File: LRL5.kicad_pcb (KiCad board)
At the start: 2 copper layers, 140 x 50 mm, 33 parts, among them J1 POWER, J2 On/Off, J5 OUT, J6 MODE, J7 ADJUST, Q1 BC549, U1 BA033CC0T, U2 NHD-C0220BIZ

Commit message: Change some pins so thay don't interact with JTAG
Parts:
- moved R8 2.00 mm to (176.2, 56.2), turned to 180 degrees
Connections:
- J3 pad 10: ADJUST_B -> unconnected-(J3-Pin_10-Pad10)
- J3 pad 11: FOUT -> unconnected-(J3-Pin_11-Pad11)
- J3 pad 12: unconnected-(J3-Pin_12-Pad12) -> MODE_B
- J3 pad 13: unconnected-(J3-Pin_13-Pad13) -> ADJUST_B
- J3 pad 9: MODE_B -> unconnected-(J3-Pin_9-Pad9)
- J4 pad 16: unconnected-(J4-Pin_16-Pad16) -> FOUT
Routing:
- net FOUT: track 26.6 -> 56.2 mm, vias 1 -> 2
- net MODE_B: track 110.9 -> 103.3 mm
- net ADJUST_B: track 51.9 -> 48.9 mm

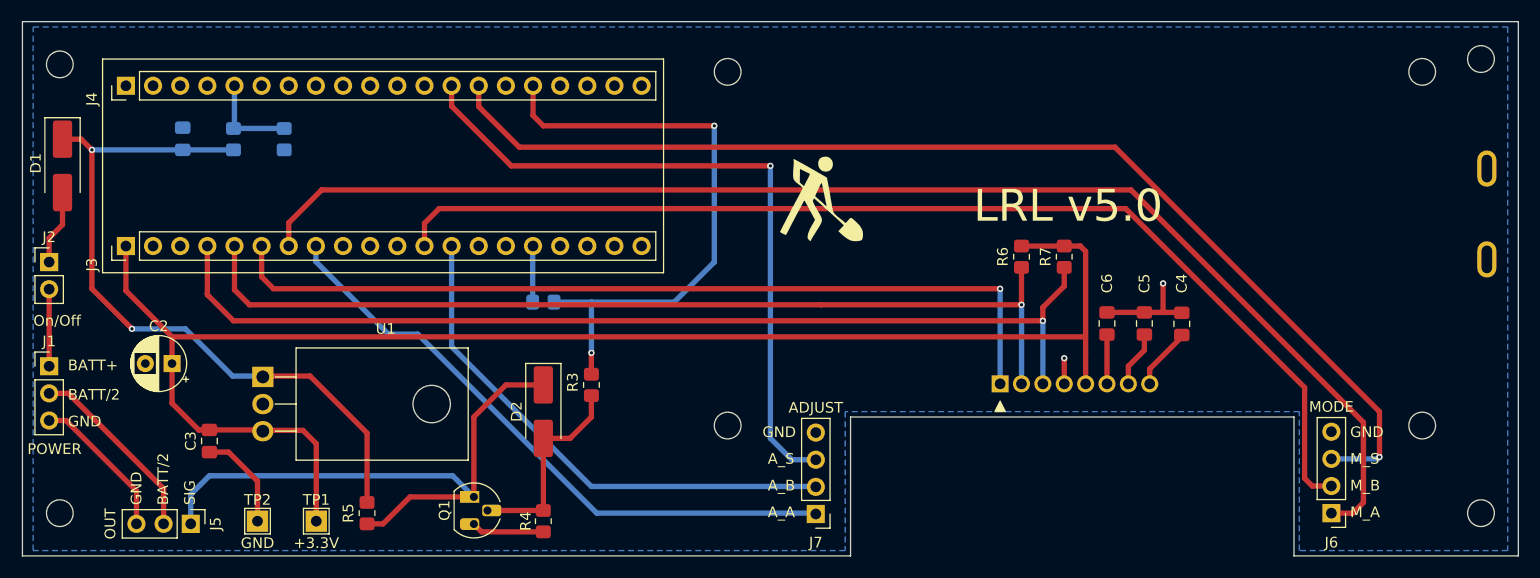
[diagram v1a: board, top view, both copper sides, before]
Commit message: Remove ADJUST connector
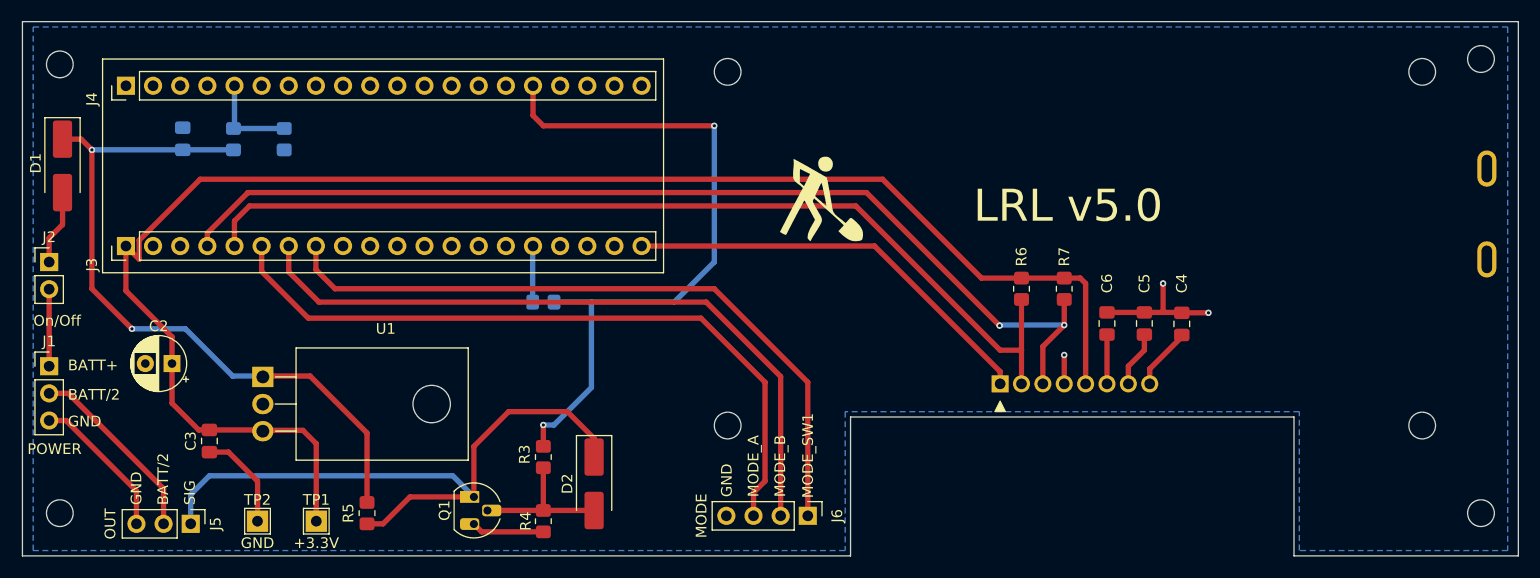
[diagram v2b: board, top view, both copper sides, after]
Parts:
- removed J7: ADJUST, Connector_PinHeader_2.54mm:PinHeader_1x04_P2.54mm_Vertical
- moved J6 49.0 mm to (201.0, 76.2), turned to -90 degrees
- moved D2 8.25 mm to (181.0, 73.2)
- moved R3 8.11 mm to (176.2, 70.8)
- moved R6 3.00 mm to (221.0, 55.0)
- moved R7 3.00 mm to (225.0, 55.0)
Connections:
- J3 pad 12: MODE_B -> unconnected-(J3-Pin_12-Pad12)
- J3 pad 13: ADJUST_B -> unconnected-(J3-Pin_13-Pad13)
- J3 pad 20: unconnected-(J3-Pin_20-Pad20) -> LCD_RESET
- J3 pad 6: LCD_RESET -> MODE_SW1
- J3 pad 7: MODE_A -> MODE_B
- J3 pad 8: ADJUST_A -> MODE_A
- J4 pad 13: ADJUST_SW1 -> unconnected-(J4-Pin_13-Pad13)
- J4 pad 14: MODE_SW1 -> unconnected-(J4-Pin_14-Pad14)
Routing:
- net ADJUST_SW1: track 64.6 -> 0.00 mm, vias 1 -> 0
- net MODE_A: track 123.9 -> 65.1 mm
- net ADJUST_A: track 58.0 -> 0.00 mm
- net ADJUST_B: track 48.9 -> 0.00 mm
- net LCD_RESET: track 81.4 -> 39.6 mm, vias 1 -> 0
- net MODE_SW1: track 107.0 -> 66.7 mm, vias 1 -> 0
- net MODE_B: track 103.3 -> 65.6 mm
- net FOUT: track 56.2 -> 65.4 mm
- net Net-(D2-A): track 19.3 -> 14.0 mm
- net Net-(D2-K): track 57.1 -> 62.0 mm
- net +3.3V: track 143.0 -> 146.8 mm
- net GND: track 43.2 -> 46.0 mm, vias 2 -> 3
- net I2C1_SDA: track 95.5 -> 96.9 mm, vias 1 -> 2
- net I2C1_SCL: track 89.3 -> 90.2 mm, vias 1 -> 0
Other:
- board text added: "+5V"
- board text added: "A0"
- board text added: "A1"
- board text added: "A10"
- board text added: "A11"
- board text added: "A12"
- board text added: "A15"
- board text added: "A2"
- board text added: "A3"
- board text added: "A4"
- board text added: "A5"
- board text added: "A6"
- board text added: "A7"
- board text added: "A8"
- board text added: "A9"
- board text added: "B0"
- board text added: "B1"
- board text added: "B10"
- board text added: "B11"
- board text added: "B12"
- board text added: "B13"
- board text added: "B14"
- board text added: "B15"
- board text added: "C13"
- board text added: "C14"
- board text added: "C15"
- board text added: "I2C1_SCL"
- board text added: "I2C1_SDA"
- board text added: "LCD_RESET"
- board text added: "PB3"
- board text added: "PB4"
- board text added: "PB5"
- board text added: "PB6"
- board text added: "PB7"
- board text added: "PB8"
- board text added: "PB9"
- board text added: "R"
- board text added: "USART1_RX"
- board text added: "USART1_TX"
- board text added: "VB"
- board text removed: "ADJUST_A"
- board text removed: "ADJUST_B"
- board text removed: "ADJUST_SW1"
- board text removed: "A_A"
- board text removed: "A_B"
- board text removed: "A_S"
- board text removed: "I2C_SCL"
- board text removed: "M_A"
- board text removed: "M_B"
- board text removed: "M_S"

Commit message: Some optimizations 3
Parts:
- moved R3 6.25 mm to (182.5, 70.8)
- moved R4 6.25 mm to (182.5, 76.8)
- moved D2 5.76 mm to (176.2, 70.0)
- moved G*** 0.50 mm to (202.0, 46.0)
- moved J5 0.50 mm to (143.2, 76.5)
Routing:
- net Net-(D2-K): track 62.0 -> 53.2 mm, vias 0 -> 1
- net GND: track 46.0 -> 51.7 mm
- net Net-(D2-A): track 14.0 -> 18.7 mm
- net FOUT: track 65.4 -> 63.7 mm
- net BATT/2: track 17.7 -> 17.2 mm
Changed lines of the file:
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@@
 	(footprint "Diode_SMD:D_SMA_Handsoldering"
 		(layer "F.Cu")
-		(at 181 73.25 -90)
+		(at 176.25 70 -90)
 		(descr "Diode SMA (DO-214AC) Handsoldering")
 		(tags "Diode SMA (DO-214AC) Handsoldering")
@@
 	(footprint "Connector_PinHeader_2.54mm:PinHeader_1x03_P2.54mm_Vertical"
 		(layer "F.Cu")
-		(at 143.25 77 -90)
+		(at 143.25 76.5 -90)
 		(descr "Through hole straight pin header, 1x03, 2.54mm pitch, single row")
 		(tags "Through hole pin header THT 1x03 2.54mm single row")
@@
 	(footprint "Resistor_SMD:R_0805_2012Metric_Pad1.20x1.40mm_HandSolder"
 		(layer "F.Cu")
-		(at 176.25 70.75 -90)
+		(at 182.5 70.75 -90)
 		(descr "Resistor SMD 0805 (2012 Metric), square (rectangular) end terminal, IPC_7351 nominal with elongated pad for handsoldering. (Body size source: IPC-SM-782 page 72, https://www.pcb-3d.com/wordpress/wp-content/uploads/ipc-sm-782a_amendment_1_and_2.pdf), generated with kicad-footprint-generator")
 		(tags "resistor handsolder")
@@
 		(tags "TO-220F-3 Horizontal RM 2.54mm")
 		(property "Reference" "U1"
-			(at -4.5 -11.5 360)
+			(at -4.5 -11.5 0)
 			(layer "F.SilkS")
 			(effects
@@
 		)
 		(fp_text user "${REFERENCE}"
-			(at -4.42 -11.5 360)
+			(at -4.42 -11.5 0)
 			(layer "F.Fab")
 			(effects
@@
 		(tags "capacitor handsolder")
 		(property "Reference" "C5"
-			(at 3.75 0 90)
+			(at 3 0 90)
 			(layer "F.SilkS")
 			(effects
@@
 		(tags "capacitor handsolder")
 		(property "Reference" "C4"
-			(at 3.7875 0 90)
+			(at 3.0375 0 90)
 			(layer "F.SilkS")
 			(effects
@@
 	(footprint "Resistor_SMD:R_0805_2012Metric_Pad1.20x1.40mm_HandSolder"
 		(layer "F.Cu")
-		(at 176.25 76.75 90)
+		(at 182.5 76.75 90)
 		(descr "Resistor SMD 0805 (2012 Metric), square (rectangular) end terminal, IPC_7351 nominal with elongated pad for handsoldering. (Body size source: IPC-SM-782 page 72, https://www.pcb-3d.com/wordpress/wp-content/uploads/ipc-sm-782a_amendment_1_and_2.pdf), generated with kicad-footprint-generator")
 		(tags "resistor handsolder")
@@
 		(tags "capacitor handsolder")
 		(property "Reference" "C6"
-			(at -3.75 0 90)
+			(at -3 0 90)
 			(layer "F.SilkS")
 			(effects
@@
 	(footprint "LOGO"
 		(layer "F.Cu")
-		(at 202 46.5)
+		(at 202 46)
 		(property "Reference" "G***"
 			(at 0 0 0)
@@
 		)
 		(fp_text user "${REFERENCE}"
-			(at 0 3.81 360)
+			(at 0 3.81 0)
 			(layer "F.Fab")
 			(effects
@@
 	)
 	(gr_text "LRL v5.0"
-		(at 216.5 49 0)
+		(at 216 46 0)
 		(layer "F.SilkS")
 		(effects
@@
 	)
 	(segment
-		(start 229 57.2125)
-		(end 234.25 57.2125)
+		(start 130 67.33)
+		(end 131.58 67.33)
 		(width 0.5)
 		(layer "F.Cu")
@@
 	)
 	(segment
-		(start 146.7875 70.2875)
-		(end 149.5 73)
+		(start 229 57.2125)
+		(end 234.25 57.2125)
 		(width 0.5)
 		(layer "F.Cu")
@@
 	)
 	(segment
-		(start 130 67.33)
-		(end 131.58 67.33)
+		(start 170.48 77.75)
+		(end 169.75 77.02)
 		(width 0.5)
 		(layer "F.Cu")
@@
 	)
 	(segment
-		(start 176.25 77.75)
+		(start 182.5 77.75)
 		(end 170.48 77.75)
 		(width 0.5)
@@
 	)
 	(segment
-		(start 234.25 54.5)
-		(end 234.25 57.2125)
+		(start 146.7875 70.2875)
+		(end 149.5 73)
 		(width 0.5)
 		(layer "F.Cu")
@@
 	)
 	(segment
-		(start 138.17 73.92)
-		(end 138.17 77)
+		(start 131.58 67.33)
+		(end 138.17 73.92)
 		(width 0.5)
 		(layer "F.Cu")
@@
 	)
 	(segment
-		(start 131.58 67.33)
-		(end 138.17 73.92)
+		(start 234.25 54.5)
+		(end 234.25 57.2125)
 		(width 0.5)
 		(layer "F.Cu")
@@
 	)
 	(segment
-		(start 234.25 57.2125)
-		(end 235.9625 57.2125)
+		(start 138.17 73.92)
+		(end 138.17 76.5)
 		(width 0.5)
 		(layer "F.Cu")
@@
 	)
 	(segment
-		(start 225 63.9)
-		(end 225 61.2)
+		(start 234.25 57.2125)
+		(end 235.9625 57.2125)
 		(width 0.5)
 		(layer "F.Cu")
@@
 	)
 	(segment
-		(start 170.48 77.75)
-		(end 169.75 77.02)
+		(start 225 63.9)
+		(end 225 61.2)
 		(width 0.5)
 		(layer "F.Cu")
@@
 	)
 	(segment
-		(start 169.75 69.75)
-		(end 173 66.5)
+		(start 169.75 72.25)
+		(end 174.5 67.5)
 		(width 0.5)
 		(layer "F.Cu")
@@
 	)
 	(segment
-		(start 173 66.5)
-		(end 178.5 66.5)
+		(start 165.52 74.48)
+		(end 163 77)
 		(width 0.5)
 		(layer "F.Cu")
@@
 	(segment
 		(start 169.75 74.48)
-		(end 163.77 74.48)
+		(end 169.75 72.5)
 		(width 0.5)
 		(layer "F.Cu")
@@
 	)
 	(segment
-		(start 169.75 74.48)
-		(end 169.75 69.75)
+		(start 163 77)
+		(end 159.75 77)
 		(width 0.5)
 		(layer "F.Cu")
@@
 	)
 	(segment
-		(start 161.25 77)
-		(end 159.75 77)
+		(start 174.5 67.5)
+		(end 176.25 67.5)
 		(width 0.5)
 		(layer "F.Cu")
@@
 	)
 	(segment
-		(start 163.77 74.48)
-		(end 161.25 77)
+		(start 169.75 72.5)
+		(end 169.75 72.25)
 		(width 0.5)
 		(layer "F.Cu")
@@
 	)
 	(segment
-		(start 181 69)
-		(end 181 70.75)
+		(start 169.75 74.48)
+		(end 165.52 74.48)
 		(width 0.5)
 		(layer "F.Cu")
 		(net 8)
 	)
-	(segment
-		(start 178.5 66.5)
-		(end 181 69)
-		(width 0.5)
-		(layer "F.Cu")
+	(via
+		(at 169.75 72.5)
+		(size 0.6)
+		(drill 0.3)
+		(layers "F.Cu" "B.Cu")
 		(net 8)
 	)
 	(segment
-		(start 143.25 74.25)
-		(end 145 72.5)
+		(start 169.75 74.48)
+		(end 169.75 72.5)
 		(width 0.5)
 		(layer "B.Cu")
@@
 	)
 	(segment
-		(start 167.77 72.5)
-		(end 169.75 74.48)
+		(start 143.25 74.25)
+		(end 145 72.5)
 		(width 0.5)
 		(layer "B.Cu")
@@
 	)
 	(segment
-		(start 143.25 77)
+		(start 143.25 76.5)
 		(end 143.25 74.25)
 		(width 0.5)
@@
 	(segment
 		(start 145 72.5)
-		(end 167.77 72.5)
+		(end 169.75 72.5)
 		(width 0.5)
 		(layer "B.Cu")
@@
 	(segment
 		(start 176.25 75.75)
-		(end 176.25 71.75)
+		(end 182.5 75.75)
+		(width 0.5)
+		(layer "F.Cu")
+		(net 9)
+	)
+	(segment
+		(start 182.5 75.75)
+		(end 182.5 71.75)
 		(width 0.5)
 		(layer "F.Cu")
@@
 	)
 	(segment
-		(start 176.25 75.75)
-		(end 181 75.75)
+		(start 176.25 72.5)
+		(end 176.25 75.75)
 		(width 0.5)
 		(layer "F.Cu")
@@
 	)
 	(segment
-		(start 131.79 64.79)
-		(end 140.71 73.71)
+		(start 140.71 73.71)
+		(end 140.71 76.5)
 		(width 0.5)
 		(layer "F.Cu")
@@
 	)
 	(segment
-		(start 140.71 73.71)
-		(end 140.71 77)
+		(start 131.79 64.79)
+		(end 140.71 73.71)
 		(width 0.5)
 		(layer "F.Cu")
@@
 	)
 	(segment
-		(start 176.25 67.75)
-		(end 176.25 69.75)
+		(start 192.25 39.75)
+		(end 176.25 39.75)
 		(width 0.5)
 		(layer "F.Cu")
@@
 	)
 	(segment
-		(start 192.25 39.75)
-		(end 176.25 39.75)
+		(start 180.75 68)
+		(end 182.5 69.75)
 		(width 0.5)
 		(layer "F.Cu")
@@
 	)
 	(via
-		(at 176.25 67.75)
+		(at 180.75 68)
 		(size 0.6)
 		(drill 0.3)
@@
 	)
 	(segment
-		(start 177.25 67.75)
-		(end 180.75 64.25)
-		(width 0.5)
-		(layer "B.Cu")
-		(net 13)
-	)
-	(segment
-		(start 180.75 64.25)
-		(end 180.75 56.25)
-		(width 0.5)
-		(layer "B.Cu")
-		(net 13)
-	)
-	(segment
 		(start 192.25 52.5)
 		(end 188.5 56.25)
@@
 	)
 	(segment
-		(start 176.25 67.75)
-		(end 177.25 67.75)
+		(start 180.75 68)
+		(end 180.75 56.25)
 		(width 0.5)
 		(layer "B.Cu")

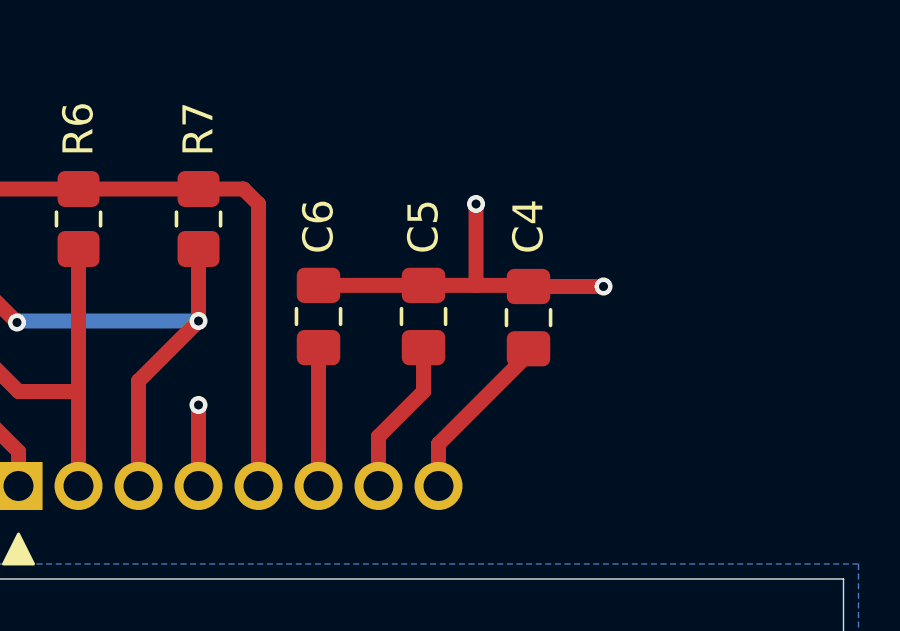
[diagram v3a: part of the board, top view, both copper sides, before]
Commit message: Fix LCD capacitor
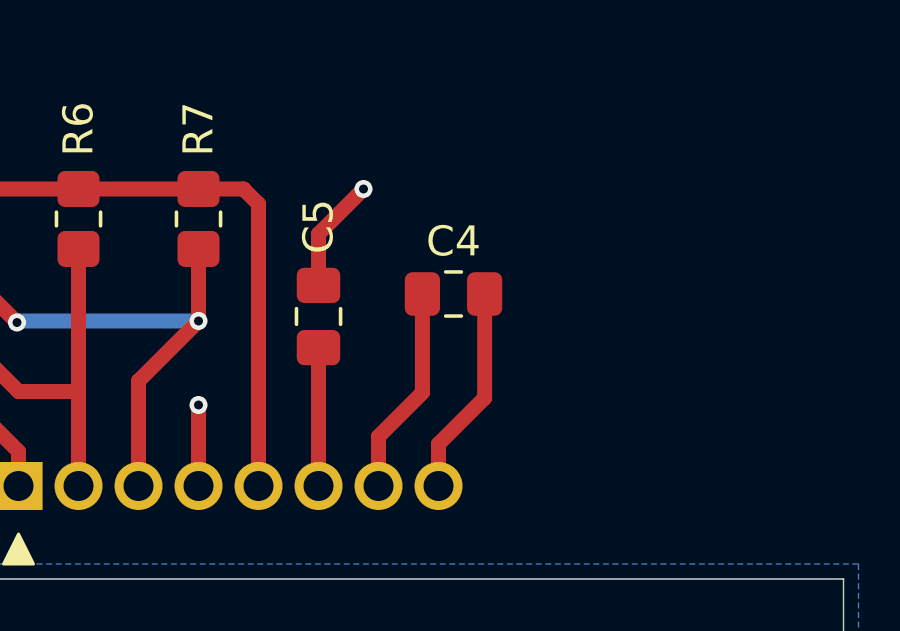
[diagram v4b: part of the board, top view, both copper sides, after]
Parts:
- removed the C5 at (232.5, 58.2)
- moved C4 2.62 mm to (233.5, 57.5), turned to 0 degrees
- renumbered C6 to C5
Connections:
- C4 pad 1: Net-(U2-C1-) -> Net-(U2-C1+)
- C4 pad 2: GND -> Net-(U2-C1-)
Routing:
- net GND: track 51.7 -> 43.4 mm, vias 3 -> 2
- net Net-(U2-C1+): track 5.23 -> 7.01 mm
- net Net-(U2-C1-): track 5.82 -> 7.04 mm
